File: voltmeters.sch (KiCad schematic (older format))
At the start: 33 parts, among them U11 LMC6482, U8 LMC6482, U9 LMC6482

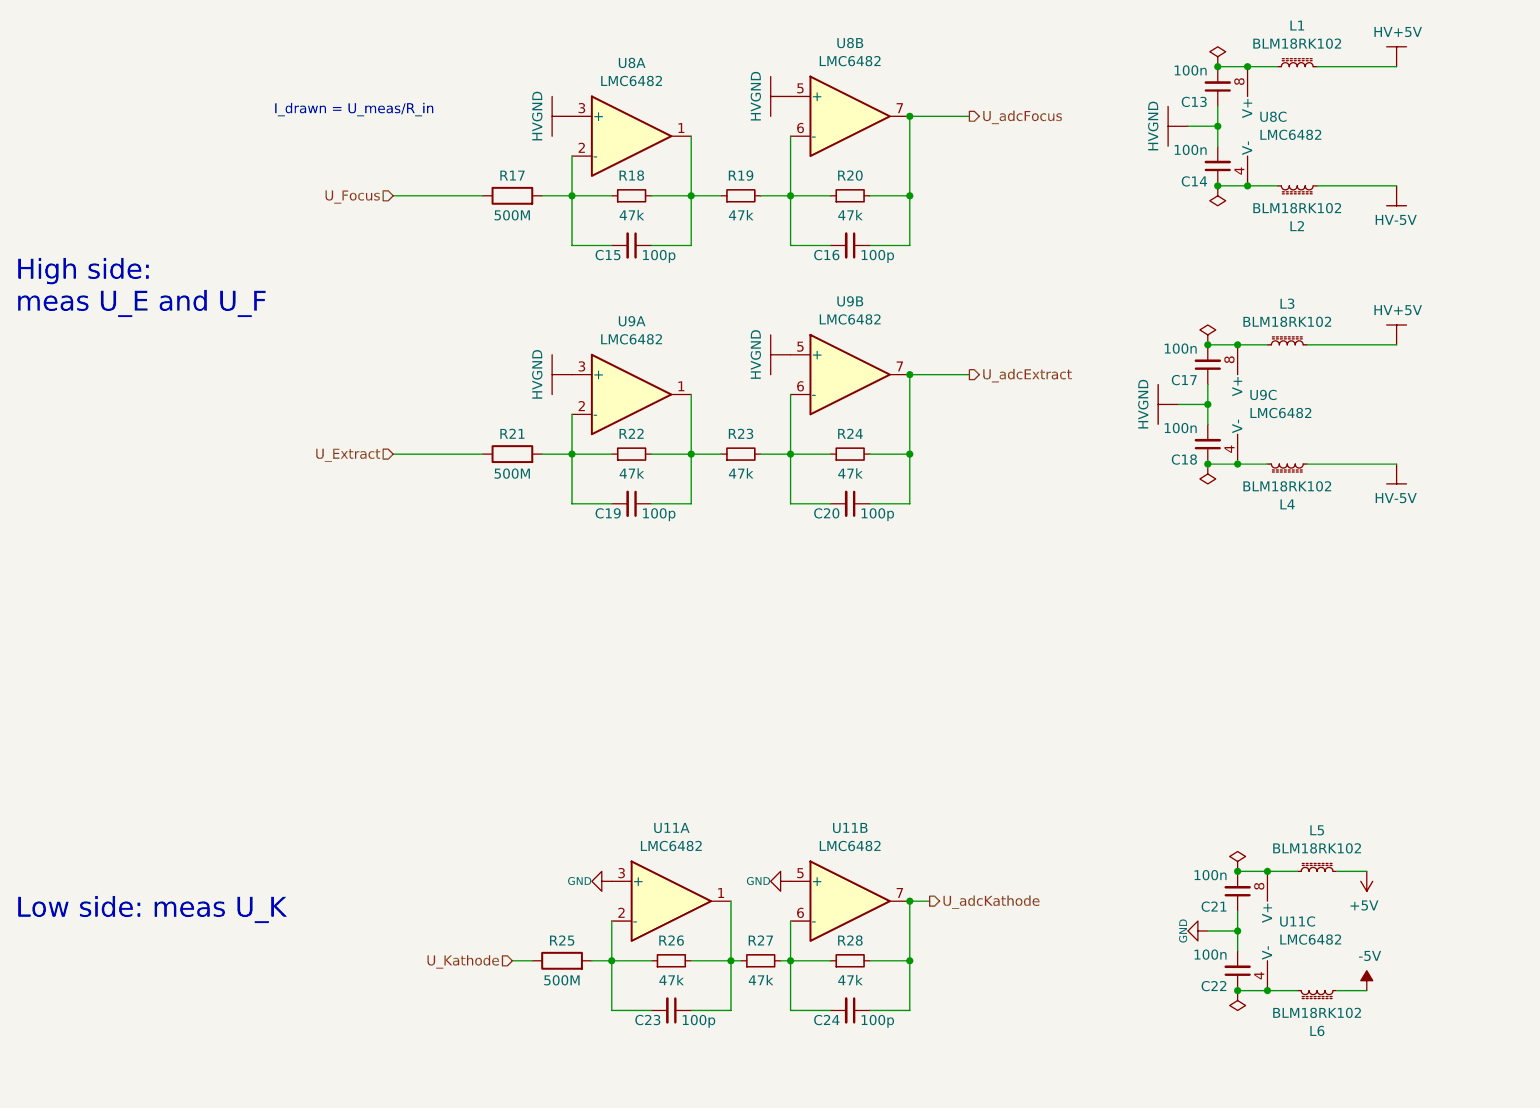
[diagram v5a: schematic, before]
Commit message: - as-built changes - add custom library elements
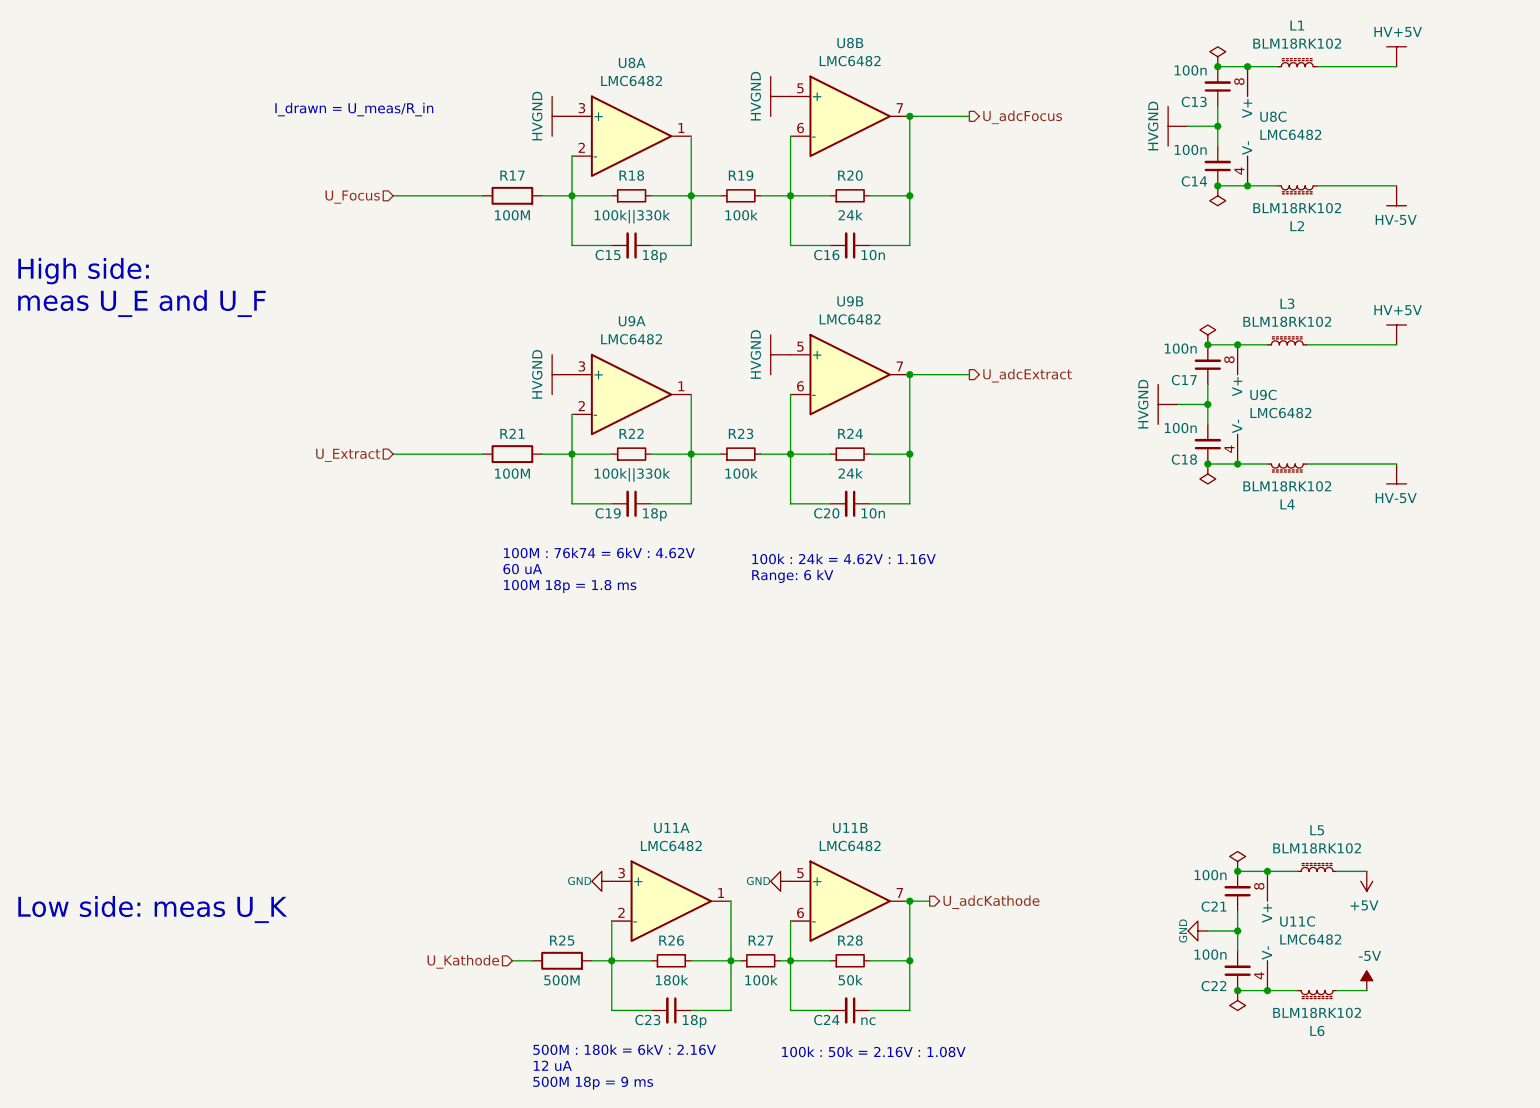
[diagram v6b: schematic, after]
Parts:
- C15, C19, C23: value 100p -> 18p
- C16, C20: value 100p -> 10n
- C24: value 100p -> nc
- R17, R21: value 500M -> 100M
- R18, R22: value 47k -> 100k||330k
- R19, R23, R27: value 47k -> 100k
- R20, R24: value 47k -> 24k
- R26: value 47k -> 180k
- R28: value 47k -> 50k
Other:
- note added: "100M : 76k74 = 6kV : 4.62V\n60 uA\n100M 18p = 1.8 ms"
- note added: "100k : 24k = 4.62V : 1.16V\nRange: 6 kV"
- note added: "100k : 50k = 2.16V : 1.08V"
- note added: "500M : 180k = 6kV : 2.16V\n12 uA\n500M 18p = 9 ms"
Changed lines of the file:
@@
 encoding utf-8
 Sheet 2 10
-Title ""
-Date ""
-Rev ""
-Comp ""
+Title "Woltomierze"
+Date "2021-01-18"
+Rev "1.0"
+Comp "Łukasz Sitarek"
 Comment1 ""
 Comment2 ""
@@
 AR Path="/5F479892/5F479BF7" Ref="R17"  Part="1"
 F 0 "R17" V 3400 1950 50  0000 C CNN
-F 1 "500M" V 3200 1950 50  0000 C CNN
+F 1 "100M" V 3200 1950 50  0000 C CNN
 F 2 "resistors_moje:MHR0317_0422_0424_0624SA" V 3230 1950 50  0001 C CNN
 F 3 "~" H 3300 1950 50  0001 C CNN
@@
 AR Path="/5F479892/5F47C5DF" Ref="C15"  Part="1"
 F 0 "C15" V 3950 2150 50  0000 R CNN
-F 1 "100p" V 3950 2250 50  0000 L CNN
+F 1 "18p" V 3950 2250 50  0000 L CNN
 F 2 "Capacitor_SMD:C_0603_1608Metric" H 3900 2200 50  0001 C CNN
 F 3 "~" H 3900 2200 50  0001 C CNN
@@
 AR Path="/5F479892/5F8ED95A" Ref="C16"  Part="1"
 F 0 "C16" V 5050 2150 50  0000 R CNN
-F 1 "100p" V 5050 2250 50  0000 L CNN
+F 1 "10n" V 5050 2250 50  0000 L CNN
 F 2 "Capacitor_SMD:C_0603_1608Metric" H 5000 2200 50  0001 C CNN
 F 3 "~" H 5000 2200 50  0001 C CNN
@@
 AR Path="/5F479892/5F8ED9C6" Ref="C20"  Part="1"
 F 0 "C20" V 5050 3450 50  0000 R CNN
-F 1 "100p" V 5050 3550 50  0000 L CNN
+F 1 "10n" V 5050 3550 50  0000 L CNN
 F 2 "Capacitor_SMD:C_0603_1608Metric" H 5000 3500 50  0001 C CNN
 F 3 "~" H 5000 3500 50  0001 C CNN
@@
 AR Path="/5F479892/5F8EDA34" Ref="C19"  Part="1"
 F 0 "C19" V 3950 3450 50  0000 R CNN
-F 1 "100p" V 3950 3550 50  0000 L CNN
+F 1 "18p" V 3950 3550 50  0000 L CNN
 F 2 "Capacitor_SMD:C_0603_1608Metric" H 3900 3500 50  0001 C CNN
 F 3 "~" H 3900 3500 50  0001 C CNN
@@
 AR Path="/5F479892/5F8F6ACD" Ref="R18"  Part="1"
 F 0 "R18" V 4000 1950 50  0000 C CNN
-F 1 "47k" V 3800 1950 50  0000 C CNN
+F 1 "100k||330k" V 3800 1950 50  0000 C CNN
 F 2 "Resistor_SMD:R_0603_1608Metric" V 3830 1950 50  0001 C CNN
 F 3 "~" H 3900 1950 50  0001 C CNN
@@
 AR Path="/5F479892/5F81E7E7" Ref="R21"  Part="1"
 F 0 "R21" V 3400 3250 50  0000 C CNN
-F 1 "500M" V 3200 3250 50  0000 C CNN
+F 1 "100M" V 3200 3250 50  0000 C CNN
 F 2 "resistors_moje:MHR0317_0422_0424_0624SA" V 3230 3250 50  0001 C CNN
 F 3 "~" H 3300 3250 50  0001 C CNN
@@
 AR Path="/5F479892/5F81FE99" Ref="R19"  Part="1"
 F 0 "R19" V 4550 1950 50  0000 C CNN
-F 1 "47k" V 4350 1950 50  0000 C CNN
+F 1 "100k" V 4350 1950 50  0000 C CNN
 F 2 "Resistor_SMD:R_0603_1608Metric" V 4380 1950 50  0001 C CNN
 F 3 "~" H 4450 1950 50  0001 C CNN
@@
 AR Path="/5F479892/5F81FEFB" Ref="R20"  Part="1"
 F 0 "R20" V 5100 1950 50  0000 C CNN
-F 1 "47k" V 4900 1950 50  0000 C CNN
+F 1 "24k" V 4900 1950 50  0000 C CNN
 F 2 "Resistor_SMD:R_0603_1608Metric" V 4930 1950 50  0001 C CNN
 F 3 "~" H 5000 1950 50  0001 C CNN
@@
 AR Path="/5F479892/5F826068" Ref="R22"  Part="1"
 F 0 "R22" V 4000 3250 50  0000 C CNN
-F 1 "47k" V 3800 3250 50  0000 C CNN
+F 1 "100k||330k" V 3800 3250 50  0000 C CNN
 F 2 "Resistor_SMD:R_0603_1608Metric" V 3830 3250 50  0001 C CNN
 F 3 "~" H 3900 3250 50  0001 C CNN
@@
 AR Path="/5F479892/5F8260E0" Ref="R23"  Part="1"
 F 0 "R23" V 4550 3250 50  0000 C CNN
-F 1 "47k" V 4350 3250 50  0000 C CNN
+F 1 "100k" V 4350 3250 50  0000 C CNN
 F 2 "Resistor_SMD:R_0603_1608Metric" V 4380 3250 50  0001 C CNN
 F 3 "~" H 4450 3250 50  0001 C CNN
@@
 AR Path="/5F479892/5F826136" Ref="R24"  Part="1"
 F 0 "R24" V 5100 3250 50  0000 C CNN
-F 1 "47k" V 4900 3250 50  0000 C CNN
+F 1 "24k" V 4900 3250 50  0000 C CNN
 F 2 "Resistor_SMD:R_0603_1608Metric" V 4930 3250 50  0001 C CNN
 F 3 "~" H 5000 3250 50  0001 C CNN
@@
 AR Path="/5FE1E896" Ref="C?"  Part="1"
 F 0 "C23" V 4150 6000 50  0000 R CNN
-F 1 "100p" V 4150 6100 50  0000 L CNN
+F 1 "18p" V 4150 6100 50  0000 L CNN
 F 2 "Capacitor_SMD:C_0603_1608Metric" H 4100 6050 50  0001 C CNN
 F 3 "~" H 4100 6050 50  0001 C CNN
@@
 AR Path="/5FE1E89D" Ref="C?"  Part="1"
 F 0 "C24" V 5050 6000 50  0000 R CNN
-F 1 "100p" V 5050 6100 50  0000 L CNN
+F 1 "nc" V 5050 6100 50  0000 L CNN
 F 2 "Capacitor_SMD:C_0603_1608Metric" H 5000 6050 50  0001 C CNN
 F 3 "~" H 5000 6050 50  0001 C CNN
@@
 AR Path="/5FE1E8B0" Ref="R?"  Part="1"
 F 0 "R26" V 4200 5800 50  0000 C CNN
-F 1 "47k" V 4000 5800 50  0000 C CNN
+F 1 "180k" V 4000 5800 50  0000 C CNN
 F 2 "Resistor_SMD:R_0603_1608Metric" V 4030 5800 50  0001 C CNN
 F 3 "~" H 4100 5800 50  0001 C CNN
@@
 AR Path="/5FE1E8B7" Ref="R?"  Part="1"
 F 0 "R27" V 4650 5800 50  0000 C CNN
-F 1 "47k" V 4450 5800 50  0000 C CNN
+F 1 "100k" V 4450 5800 50  0000 C CNN
 F 2 "Resistor_SMD:R_0603_1608Metric" V 4480 5800 50  0001 C CNN
 F 3 "~" H 4550 5800 50  0001 C CNN
@@
 AR Path="/5FE1E8BE" Ref="R?"  Part="1"
 F 0 "R28" V 5100 5800 50  0000 C CNN
-F 1 "47k" V 4900 5800 50  0000 C CNN
+F 1 "50k" V 4900 5800 50  0000 C CNN
 F 2 "Resistor_SMD:R_0603_1608Metric" V 4930 5800 50  0001 C CNN
 F 3 "~" H 5000 5800 50  0001 C CNN
@@
 $EndComp
 Connection ~ 6950 5950
+Text Notes 3400 6450 0    50   ~ 0
+500M : 180k = 6kV : 2.16V\n12 uA\n500M 18p = 9 ms
+Text Notes 4650 6300 0    50   ~ 0
+100k : 50k = 2.16V : 1.08V
+Text Notes 3250 3950 0    50   ~ 0
+100M : 76k74 = 6kV : 4.62V\n60 uA\n100M 18p = 1.8 ms
+Text Notes 4500 3900 0    50   ~ 0
+100k : 24k = 4.62V : 1.16V\nRange: 6 kV
 $EndSCHEMATC
